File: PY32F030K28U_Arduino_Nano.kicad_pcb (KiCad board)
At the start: 2 copper layers, 43.2 x 17.8 mm, 28 parts, among them J1 USB_C_Receptacle_USB2.0, J2 DAPLINK, Q1 AO3401A, Q2 2N7002DW, SW1 SW_Push, SW2 SW_Push, U1 ME6211CxxU4AG, U2 PY32F030K2xU, U3 CH343P, U4 Arduino Nano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

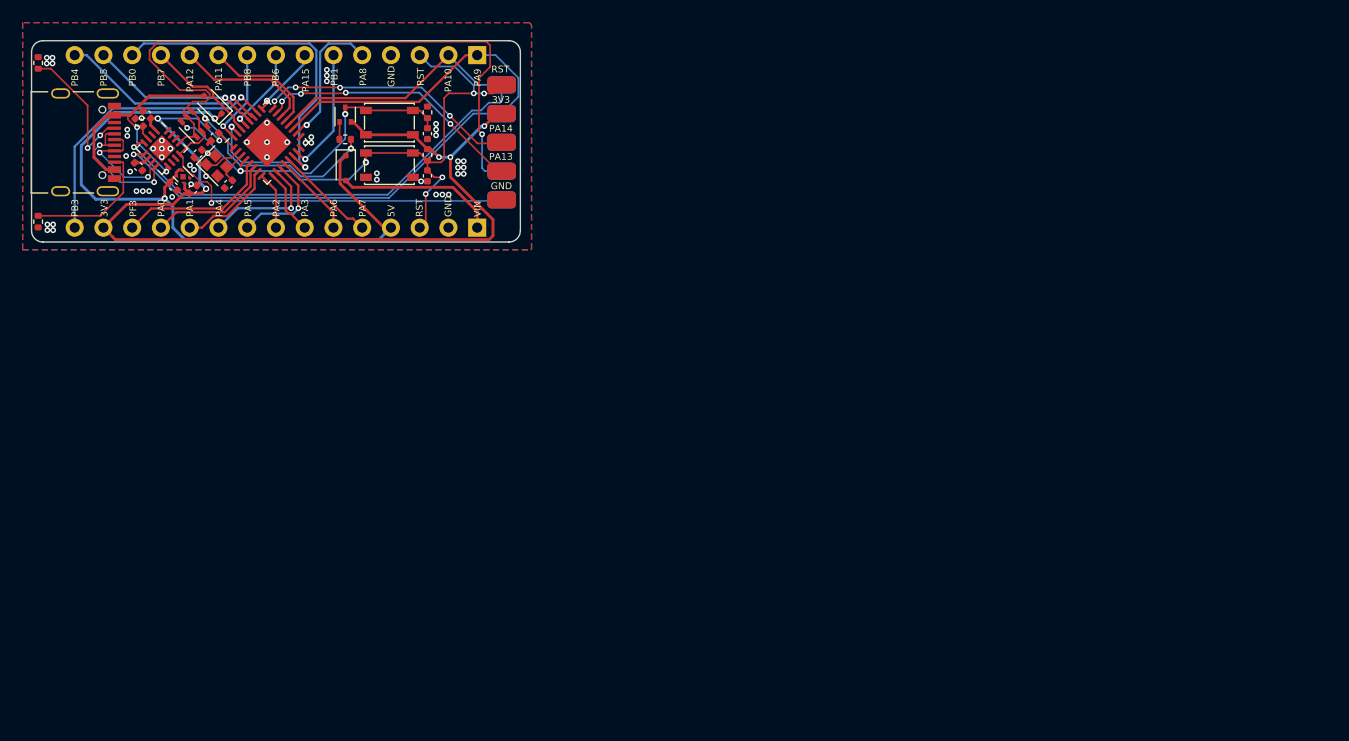
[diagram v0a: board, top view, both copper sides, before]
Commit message: corrected DRC errors in PCB design
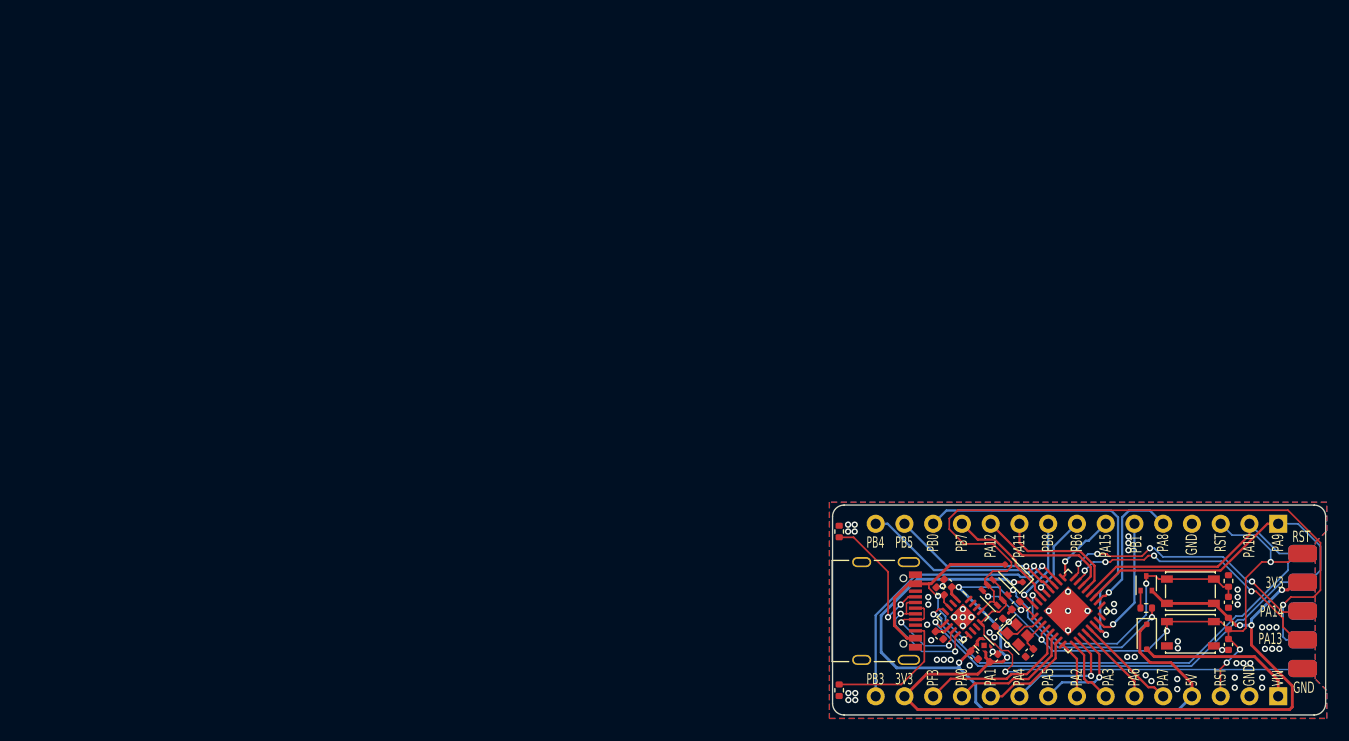
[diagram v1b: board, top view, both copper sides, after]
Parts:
- moved C10 82.0 mm to (105.3, 70.5)
- moved C8 82.0 mm to (98.1, 64.3)
- moved D1 82.0 mm to (103.9, 63.4)
- moved J1 82.0 mm to (92.7, 66.8)
- moved SW1 82.0 mm to (119.5, 65.0)
- moved SW2 82.0 mm to (119.5, 68.8)
- moved U2 82.0 mm to (108.7, 66.8)
- moved U3 82.0 mm to (99.4, 67.3)
- moved U4 82.0 mm to (87.9, 75.6)
- moved C1 82.0 mm to (100.4, 70.7)
- moved C2 82.0 mm to (102.2, 70.9)
- moved C3 82.0 mm to (104.1, 66.3)
- moved C4 82.0 mm to (122.9, 69.7)
- moved C5 82.0 mm to (122.9, 66.0)
- moved C6 82.0 mm to (97.3, 68.9)
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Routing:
- net /RTS: track 58.7 -> 62.1 mm
- net +5V: track 59.8 -> 61.2 mm
- net /NRST: track 53.5 -> 52.3 mm, vias 7 -> 6
- net +3V3: track 89.4 -> 90.5 mm
- net /PA11: track 10.6 -> 11.6 mm
- net /DTR: track 37.2 -> 38.1 mm
- net /PA14: track 23.1 -> 23.9 mm
- net /PA10: track 62.6 -> 63.4 mm
- net /PA13: track 23.5 -> 24.2 mm
- net /PA9: track 65.4 -> 66.1 mm
- net Net-(Q2B-D): track 18.2 -> 17.6 mm
- net GND: vias 53 -> 63
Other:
- board size 43.2 x 17.8 mm -> 43.6 x 18.5 mm
- board text added: "RTS"

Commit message: improved PCB design file
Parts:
- C1, C10, C2, C3, C4, C5, C6, C7, C8, C9: footprint Capacitor_SMD:C_0402_1005Metric -> footprints:C_0402_1005Metric
- D1, D2: footprint Diode_SMD:D_SOD-323F -> footprints:D_SOD-323F
- J1: footprint Connector_USB:USB_C_Receptacle_Palconn_UTC16-G -> footprints:USB_C_Receptacle_Palconn_UTC16-G
- J2: footprint AirM2M:DAPLink-port -> footprints:DAPLink-port
- Q1: footprint Package_TO_SOT_SMD:SOT-523 -> footprints:SOT-523
- Q2: footprint Package_TO_SOT_SMD:SOT-363_SC-70-6 -> footprints:SOT-363_SC-70-6
- R1, R2, R3, R4, R7: footprint Resistor_SMD:R_0402_1005Metric -> footprints:R_0402_1005Metric
- SW1, SW2: footprint Button_Switch_SMD:SW_SPST_PTS810 -> footprints:SW_SPST_PTS810
- U1: footprint Package_DFN_QFN:UDFN-4-1EP_1x1mm_P0.65mm_EP0.48x0.48mm -> footprints:UDFN-4-1EP_1x1mm_P0.65mm_EP0.48x0.48mm
- U2: footprint Package_DFN_QFN:QFN-32-1EP_5x5mm_P0.5mm_EP3.1x3.1mm -> footprints:QFN-32-1EP_5x5mm_P0.5mm_EP3.1x3.1mm
- U3: footprint Package_DFN_QFN:QFN-16-1EP_3x3mm_P0.5mm_EP1.7x1.7mm -> footprints:QFN-16-1EP_3x3mm_P0.5mm_EP1.7x1.7mm
- U4: footprint Arduino Board:Arduino Nano -> footprints:Arduino Nano
- Y1: footprint Crystal:Crystal_SMD_2016-4Pin_2.0x1.6mm -> footprints:Crystal_SMD_2016-4Pin_2.0x1.6mm
- moved R1 0.53 mm to (89.0, 59.7)
- moved R2 0.53 mm to (89.0, 73.8)
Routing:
- net Net-(Q2B-D): track 17.6 -> 19.0 mm
- net /NRST: track 52.3 -> 53.1 mm
- net Net-(J1-CC1): track 12.8 -> 12.2 mm
- net Net-(J1-CC2): track 11.8 -> 11.3 mm
- net GND: track 0.47 -> 0.00 mm, vias 63 -> 94
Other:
- board text added: "BOOT0"
- board text added: "CLK"
- board text added: "DIO"
- board text added: "RESET"
- board text added: "RX/PA10"
- board text added: "TX/PA9"
- board text removed: "PA13"
- board text removed: "PA14"
